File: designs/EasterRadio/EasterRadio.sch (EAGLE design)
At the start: 4 parts

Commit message: go
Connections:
- net N$1 renamed ROUT
- new net +OUT_L: JP3.1
- new net +OUT_R: JP4.8
- new net -OUT_L: JP3.3
- new net -OUT_R: JP4.6
- new net AGND: JP2.3, JP2.4, JP3.2, JP4.1, JP4.3, JP4.7
- new net AMI: JP1.12
- new net BAND: JP1.5
- new net DBYP: JP2.12
- new net FMI: JP1.8
- new net INL: JP3.7
- new net INR: JP4.2
- new net IRQ: JP1.2
- new net LNA_EN: JP1.1
- new net MUTE: JP3.5
- new net NC: JP1.6
- new net NC1: JP1.7
- new net NC2: JP1.10
- new net NC3: JP1.11
- new net PVDD: JP3.4
- new net PVDD2: JP4.5
- new net RFGND: JP1.9
- new net RST: JP2.5
- new net SCLK: JP2.7
- new net SDIO: JP2.6
- new net SHDN: JP4.4
- new net TUNE1: JP1.3
- new net TUNE2: JP1.4
- new net VDD: JP3.6
- new net VDD1: JP2.10
- new net VDD2: JP2.11
- new net VREF: JP3.8
- new net XTALI: JP2.9
- new net XTALO: JP2.8

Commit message: finished PAM8403 schematic
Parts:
- removed JP1, JP2: (no value), pinhead:PINHD-1X14
- added C1, C2, C5: 1uF, CommonParts:C-EU_805C0805
- added C3, C4: 0.47uF, CommonParts:C-EU_805C0805
- added C6: 0.1uF, CommonParts:C-EU_805C0805
- added C7, C8: 470uF, CommonParts:C-EU_805C0805
- added J1, J2: S2B-NSHSS-TB, CommonParts:S2B-NSHSS-TB
- added JP5, JP6: (no value), pinhead:PINHD-1X14
- added R1, R2: 10k, CommonParts:R-EU_805R0805
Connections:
- removed net PVDD: JP3.4
- removed net PVDD2: JP4.5
- removed net VDD: JP3.6
- new net N$1: C3.1, R1.2
- new net N$4: C4.2, R2.2
- new net VDD3.3V: C1.1, C2.2, C5.1, C7.1, C8.2, JP3.4, JP3.6, JP4.5
- net +OUT_L: now also J2.2
- net +OUT_R: now also J1.2
- net -OUT_L: now also J2.1
- net -OUT_R: now also J1.1
- net AGND: now also C1.2, C2.1, C5.2, C6.2, C7.2, C8.1, JP6.3, JP6.4; no longer JP2.3, JP2.4
- net AMI: now also JP5.12; no longer JP1.12
- net BAND: now also JP5.5; no longer JP1.5
- net DBYP: now also JP6.12; no longer JP2.12
- net FMI: now also JP5.8; no longer JP1.8
- net INL: now also C4.1, R2.1
- net INR: now also R1.1
- net IRQ: now also JP5.2; no longer JP1.2
- net LNA_EN: now also JP5.1; no longer JP1.1
- net LOUT: now also JP6.14; no longer JP2.14
- net NC: now also JP5.6; no longer JP1.6
- net NC1: now also JP5.7; no longer JP1.7
- net NC2: now also JP5.10; no longer JP1.10
- net NC3: now also JP5.11; no longer JP1.11
- net RFGND: now also JP5.9; no longer JP1.9
- net ROUT: now also JP6.13; no longer JP2.13
- net RST: now also JP6.5; no longer JP2.5
- net SCLK: now also JP6.7; no longer JP2.7
- net SDIO: now also JP6.6; no longer JP2.6
- net TUNE1: now also JP5.3; no longer JP1.3
- net TUNE2: now also JP5.4; no longer JP1.4
- net VDD1: now also JP6.10; no longer JP2.10
- net VDD2: now also JP6.11; no longer JP2.11
- net VREF: now also C6.1
- net XTALI: now also JP6.9; no longer JP2.9
- net XTALO: now also JP6.8; no longer JP2.8

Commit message: Working Progress for Si4844 radio ic
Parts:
- added C10, C15: 1uF, CommonParts:C-EU_805C0805
- added C11, C9: 1nF, CommonParts:C-EU_805C0805
- added C12: 100uF, CommonParts:C-EU_1206C1206
- added C13: 20nF, CommonParts:C-EU_805C0805
- added C14: 4.7uF, CommonParts:C-EU_1206C1206
- added C16, C17: 22p, CommonParts:C-EU_805C0805
- added EN, RST: FSMSMTR, FSMSMTR:FSMSMTR
- added IC6: ESP32-WROVER-B, ESP32-WROVER-B:ESP32-WROVER-B
- added J3, J5: S2B-NSHSS-TB, CommonParts:S2B-NSHSS-TB
- added JTAG: 1, con-lstb:MA04-1
- added LED1: (no value), led:LEDSMT1206
- added ON/OFF: -CON3, tango:-CON3
- added POWER: S2B-PH-SM4-TB, S2B-PH-SM4-TB:S2B-PH-SM4-TB
- added R3: 12k, CommonParts:R-EU_805R0805
- added R4: 460ohm, CommonParts:R-EU_805R0805
- added R5: 10K, CommonParts:R-EU_1206R1206
- added R6: 1K, rcl:R-EU_R1206
- added UART: 057-006-1, con-panduit:057-006-1
- added Y1: 32.768kHz crystal, MouserUseful:CM7V-T1A-32.768K-9PF-20PPM-TA-
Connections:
- removed net NC2: JP5.10
- removed net NC3: JP5.11
- removed net RFGND: JP5.9
- removed net VDD1: JP6.10
- removed net VDD2: JP6.11
- new net 3.3V: C10.1, C12.1, IC6.VDD33, J5.2, ON/OFF.1, R3.2, R5.1, R6.2, UART-3.S, UART-4.S
- new net CLK: IC6.CLK
- new net CMD: IC6.CMD
- new net EN: C11.1, C9.1, EN.2, IC6.EN, R3.1, R4.1, R4.2
- new net GND: C10.2, C11.2, C12.2, C13.2, C9.2, EN.1, IC6.GND_1, IC6.GND_2, IC6.GND_3, IC6.GND_4, J3.1, J5.1, LED1.C, POWER.1, RST.2, UART-2.S, UART-5.S
- new net GPIO12: IC6.IO12, JTAG.2
- new net GPIO13: IC6.IO13, JTAG.3
- new net GPIO14: IC6.IO14, JTAG.1
- new net GPIO15: IC6.IO15, JTAG.4
- new net IO0: IC6.IO0, RST.1
- new net IO18: IC6.IO18
- new net IO19: IC6.IO19
- new net IO2: IC6.IO2
- new net IO21: IC6.IO21
- new net IO22: IC6.IO22
- new net IO23: IC6.IO23
- new net IO25: IC6.IO25
- new net IO26: IC6.IO26
- new net IO27: IC6.IO27
- new net IO32: IC6.IO32
- new net IO33: IC6.IO33
- new net IO34: IC6.IO34
- new net IO35: IC6.IO35
- new net IO4: IC6.IO4
- new net IO5: IC6.IO5
- new net N$14: LED1.A, R6.1
- new net N$2: ON/OFF.2, POWER.2
- new net NC_1: IC6.NC_1
- new net NC_2: IC6.NC_2
- new net NC_3: IC6.NC_3
- new net RXD0: C13.1, IC6.RXD0, J3.2, R5.2, UART-1.S
- new net SD0: IC6.SD0
- new net SD1: IC6.SD1
- new net SD2: IC6.SD2
- new net SD3: IC6.SD3
- new net SEN_VN: IC6.SENSOR_VN
- new net SEN_VP: IC6.SENSOR_VP
- new net TXD0: IC6.TXD0, UART-6.S
- new net VDD: C14.1, C15.1, JP6.10, JP6.11
- net AGND: now also C16.1, C17.1, JP5.10, JP5.11, JP5.9
- net DBYP: now also C14.2, C15.2
- net XTALI: now also C17.2, Y1.1
- net XTALO: now also C16.2, Y1.2
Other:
- note added: "I2C: IO22 SCL IO21 SDA"

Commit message: added charging ic and radio fm/am chip
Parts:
- added B1: 2.5K, CommonParts:C-EU_805C0805
- added C18: 33pF, CommonParts:C-EU_805C0805
- added C19: 33nF, CommonParts:C-EU_1206C1206
- added C20, C22: .47nF, CommonParts:C-EU_805C0805
- added C21: 33nF, MouserUseful:CNC5L1X7R1C106K160AEC1206
- added C23: .47uF, CommonParts:C-EU_805C0805
- added C24: 47uF, MouserUseful:CNC5L1X7R1C106K160AEC1206
- added C25: .1nF, CommonParts:C-EU_805C0805
- added C26, C27: 4.7uF, CommonParts:C-EU_1206C1206
- added C28: 100nF, CommonParts:C-EU_1206C1206
- added C29: 10uF, CommonParts:C-EU_1206C1206
- added IC1: MCP73832T-2ACI_OT, MouserUseful:MCP73832T-2ACI_OT
- added IC2: LD117ADT-TR, nixie_tube:LD117ADT-TR
- added J4: S2B-PH-SM4, CommonParts:S2B-PH-SM4
- added J6: PJ-002AH-SMT-TR, CommonParts:PJ-002AH-SMT-TR
- added L1: 270nH, MouserUseful:LQW2UASR56F0CL
- added LED2: (no value), CommonParts:LED_1206SMT1206
- added Q1: 2SC3838T146, transistor-small-signal:2SC3838T146
- added R10: 10K, MouserUseful:RCS1206100KJNEAR1206
- added R11: 100, MouserUseful:ERJ-PB6B5623VR0805
- added R12: Data Sheet, CommonParts:R-EU_1206R1206
- added R13: 470ohm, CommonParts:R-EU_1206R1206
- added R7: 120k, MouserUseful:ERJ-PB6B5623VR0805
- added R8: 100k, MouserUseful:ERJ-PB6B5623VR0805
- added R9: 1K, MouserUseful:RCS1206100KJNEAR1206
- added VR1: RK09D113BF25B15, MouserUseful:RK09D113BF25B15
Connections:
- new net +ANT1: C22.1, C23.1
- new net 12V: C28.1, IC2.IN, J6.1_1, J6.1_2
- new net 5V: C27.1, C29.1, IC1.VDD, IC2.OUT, LED2.A
- new net ANT2: B1.1, C18.2
- new net GNDA: C26.1, C27.2, C28.2, C29.2, IC1.VSS, IC2.ADJ, J4.2, J4.SHIELD, J6.2, J6.3, R12.2
- new net N$10: LED2.C, R13.2
- new net N$3: B1.2, C19.1
- new net N$5: C19.2, Q1.B, R7.1, R8.2
- new net N$6: C22.2, Q1.C, R9.1
- new net N$7: C21.2, R10.1, R9.2
- new net N$8: C20.1, R10.2
- new net N$9: R11.2, VR1.3
- new net PROG: IC1.PROG, R12.1
- new net STAT: IC1.STAT, R13.1
- new net VBAT: C26.2, IC1.VBAT, J4.1
- net AGND: now also C20.2, C21.1, C24.2, C25.1, L1.1, Q1.E, R11.1, R8.1
- net AMI: now also C23.2
- net FMI: now also C18.1, L1.2
- net LNA_EN: now also R7.2
- net TUNE1: now also C24.1, C25.2, VR1.1
- net TUNE2: now also VR1.2

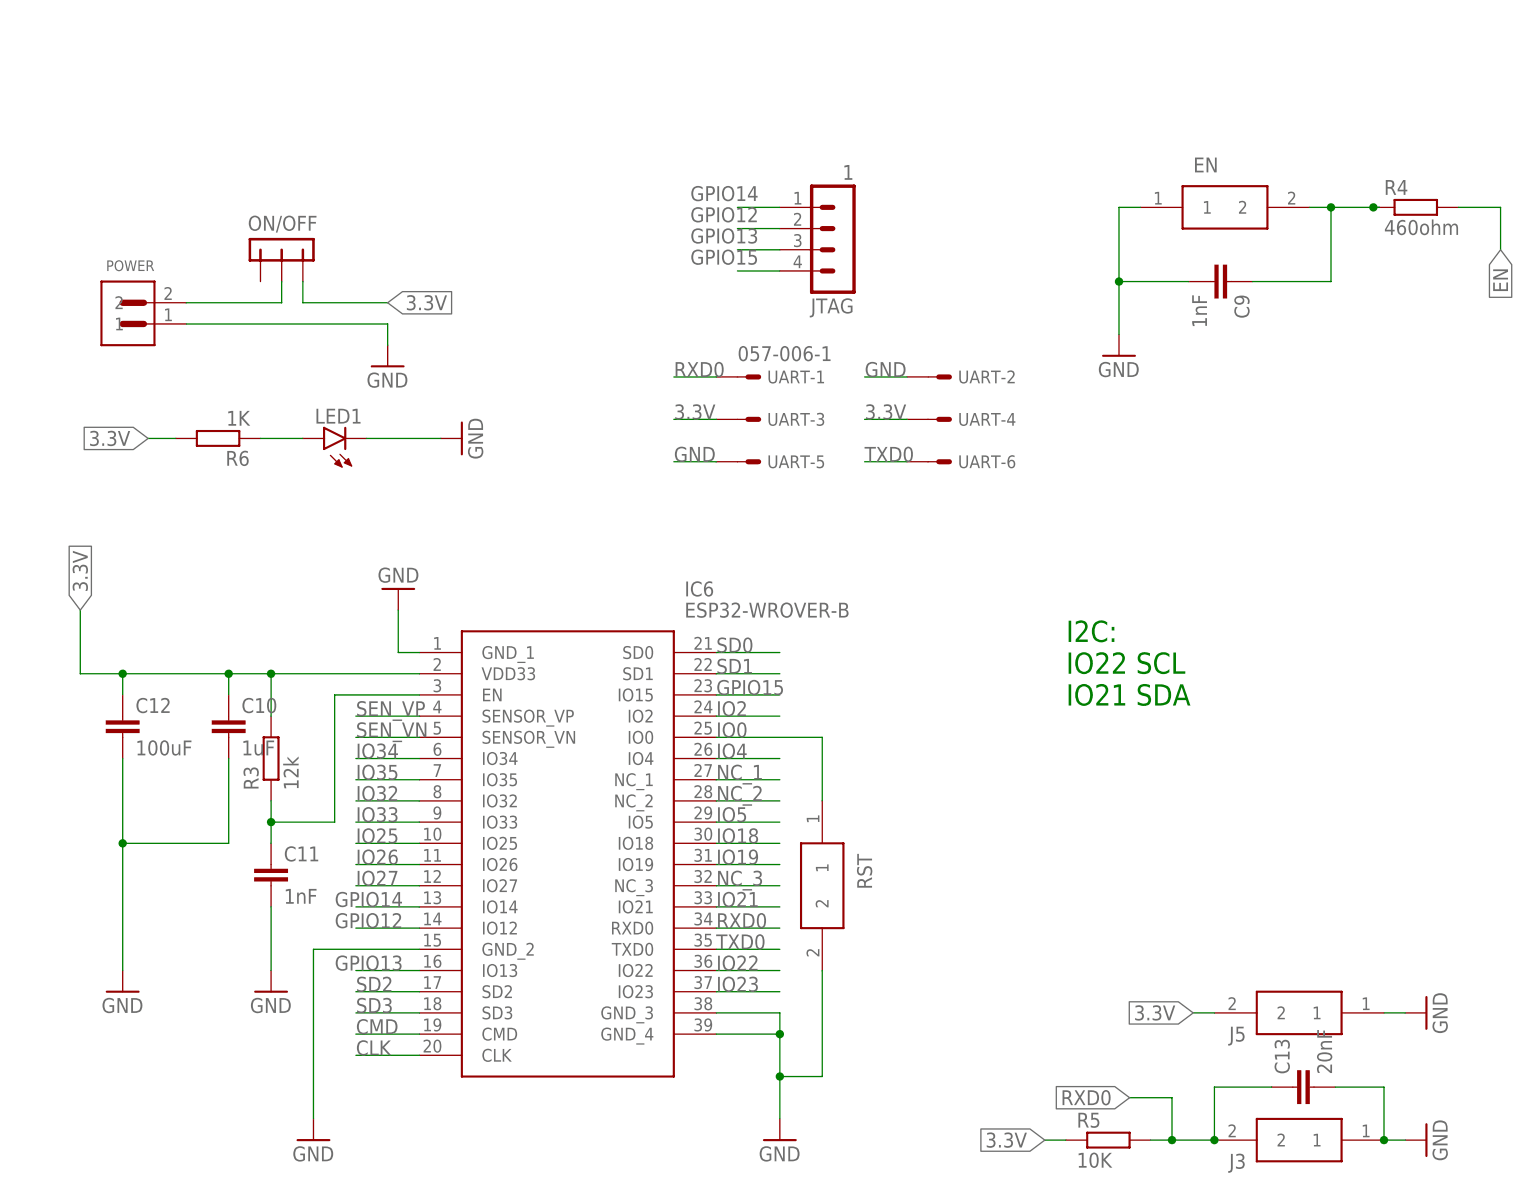
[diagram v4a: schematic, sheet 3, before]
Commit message: added pins for different sheet connections
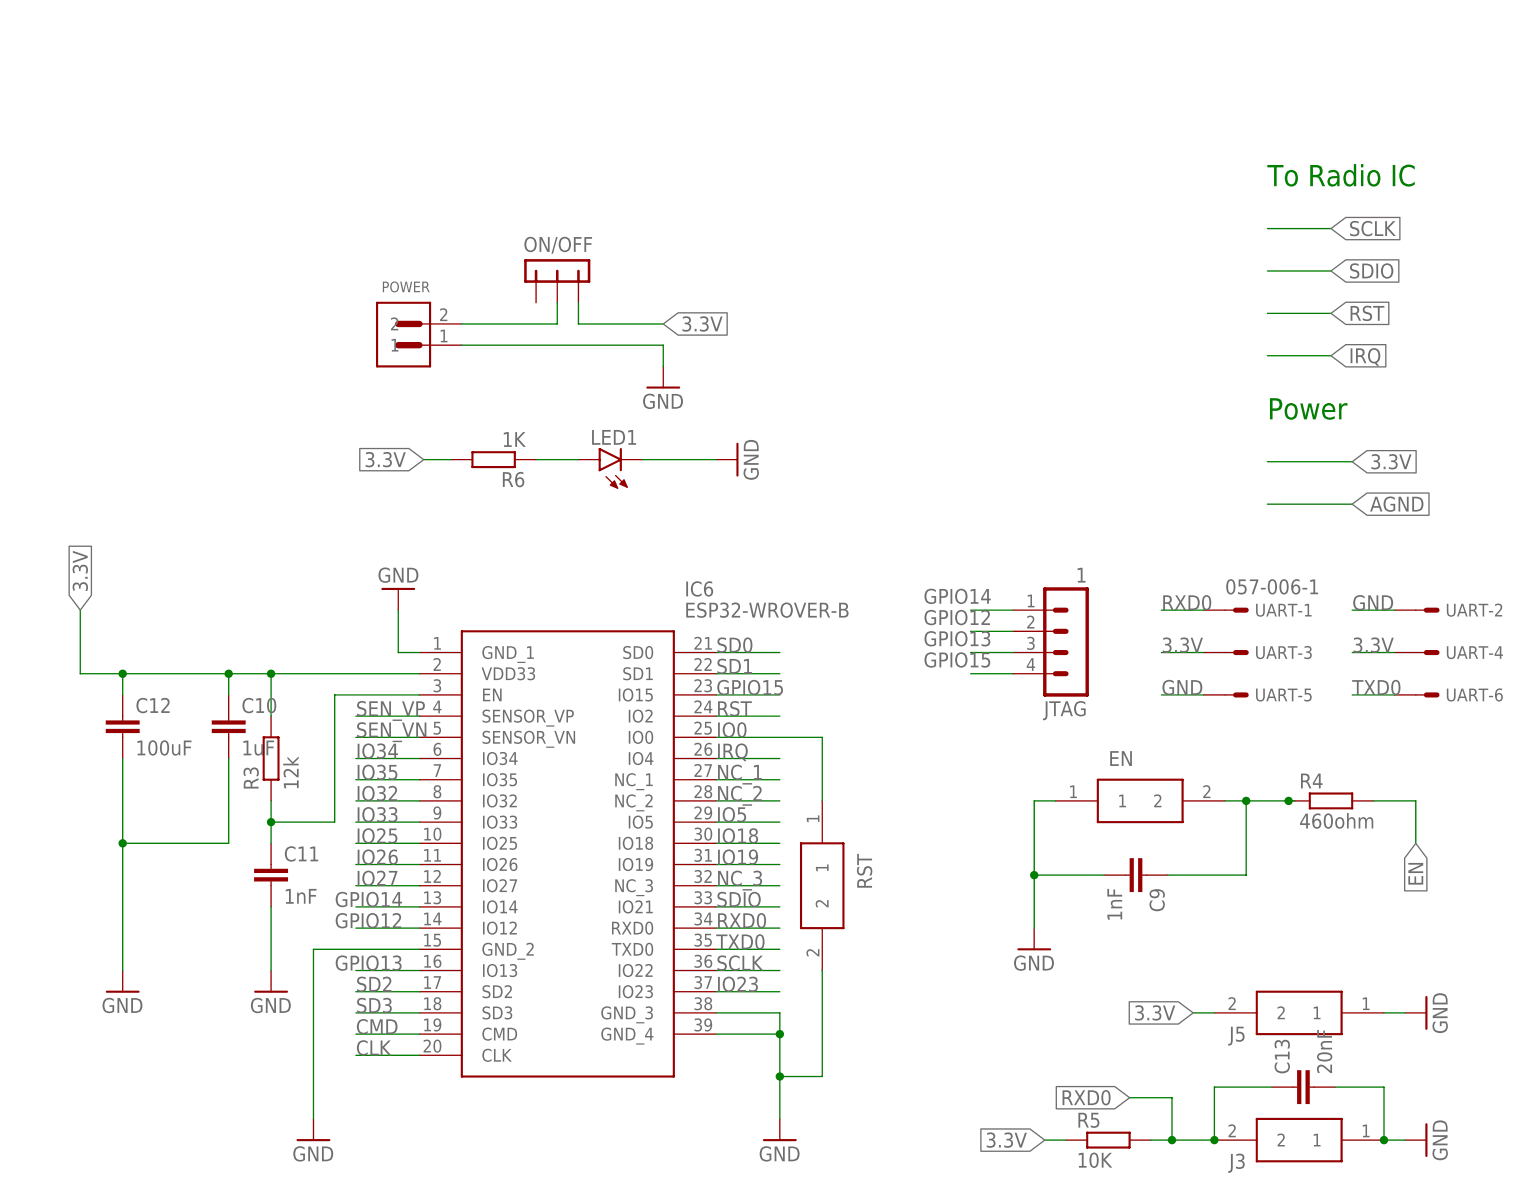
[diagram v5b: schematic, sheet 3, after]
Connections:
- removed net IO2: IC6.IO2
- removed net IO21: IC6.IO21
- removed net IO22: IC6.IO22
- removed net IO4: IC6.IO4
- removed net LOUT: JP6.14
- removed net MUTE: JP3.5
- removed net ROUT: JP6.13
- removed net SHDN: JP4.4
- removed net VDD3.3V: C1.1, C2.2, C5.1, C7.1, C8.2, JP3.4, JP3.6, JP4.5
- net 3.3V: now also C1.1, C2.2, C5.1, C7.1, C8.2, JP3.4, JP3.5, JP3.6, JP4.4, JP4.5
- net INL: now also JP6.14
- net INR: now also C3.2, JP6.13
- net IRQ: now also IC6.IO4
- net RST: now also IC6.IO2
- net SCLK: now also IC6.IO22
- net SDIO: now also IC6.IO21
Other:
- note added: "Power"
- note added: "To Amplifier"
- note added: "To ESP32"
- note added: "To Radio Chip"
- note added: "To Radio IC"
- note removed: "I2C: IO22 SCL IO21 SDA"
- moved on the sheet: C9, EN, JTAG, LED1, ON/OFF, POWER, R4, R6, UART-1, UART-2, UART-3, UART-4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

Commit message: added load to battery in Lipo Charger IC
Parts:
- added C30: 1uF, CommonParts:C-EU_805C0805
- added D1: 1N4942, diode:1N4942
- added IC3: DMP1045U-7, MouserUseful:DMP1045U-7
- added JP1: (no value), pinhead:PINHD-1X4
- added R14: 100K, CommonParts:R-EU_1206R1206
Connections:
- net 12V: now also C30.1, D1.C, IC3.D, JP1.1
- net 3.3V: now also JP1.4
- net 5V: now also D1.A, IC3.G, R14.1
- net GNDA: now also C30.2, JP1.2, JP1.3, R14.2
- net VBAT: now also IC3.S
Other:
- note added: "Amplifier (PAM8403DR)"
- note added: "Battery Management (MCP73832T-2ACI/OT)"
- note added: "ESP32 (ESP32-Wrover-B)"
- note added: "Radio IC (SI4840-A10-GU)"
- moved on the sheet: C28, C29, IC2, J6
